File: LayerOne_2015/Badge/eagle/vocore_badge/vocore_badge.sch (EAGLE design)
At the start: 22 parts, among them U1 FT232RL-BASICSSOP

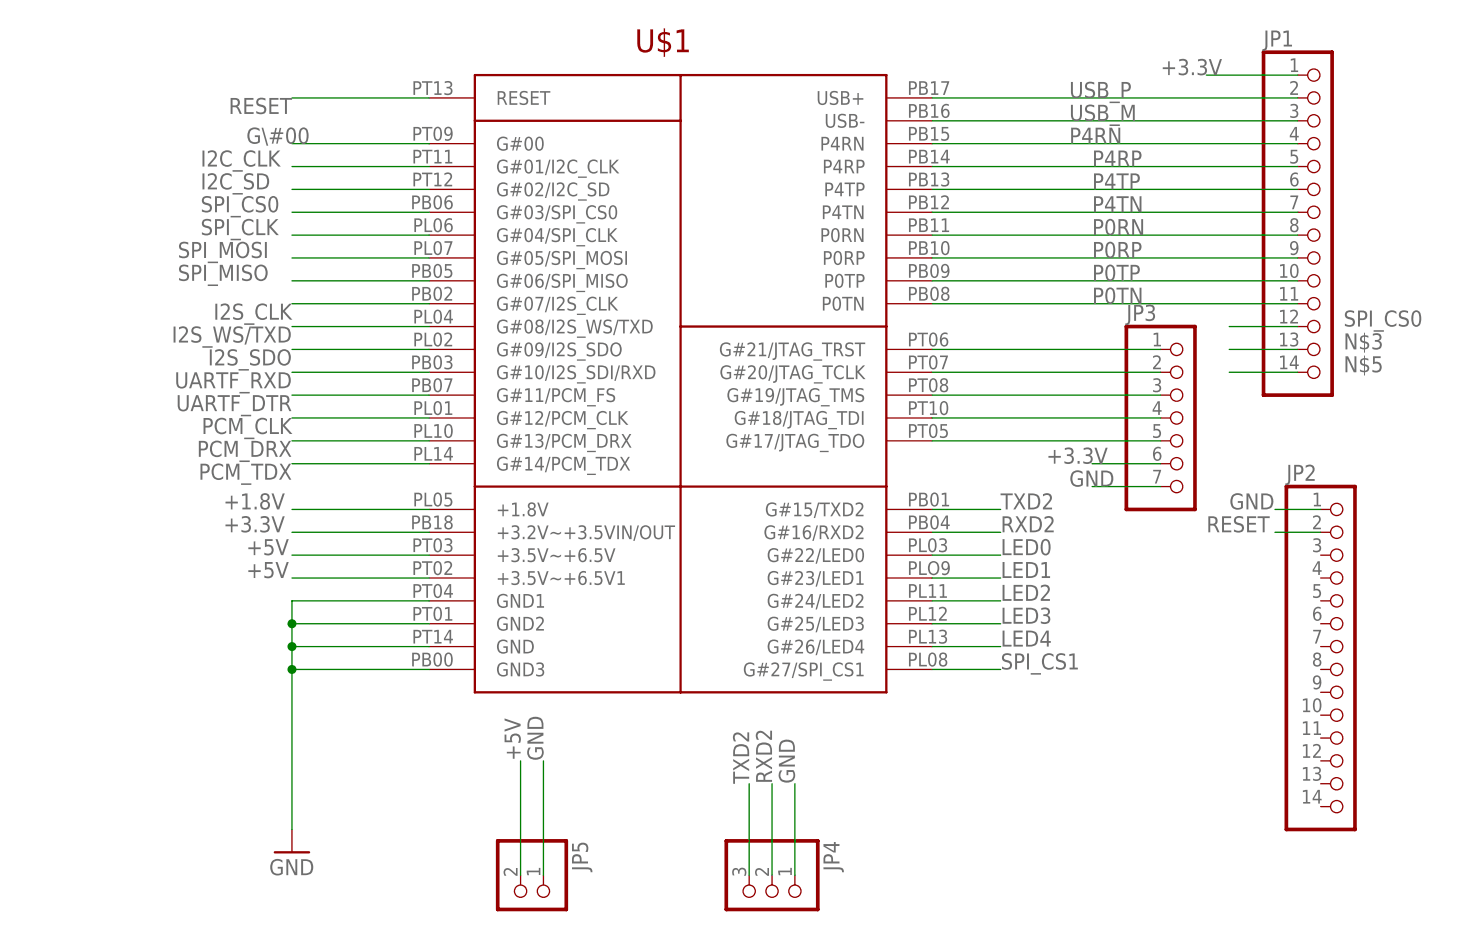
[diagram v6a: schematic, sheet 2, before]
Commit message: more breakouts on dock
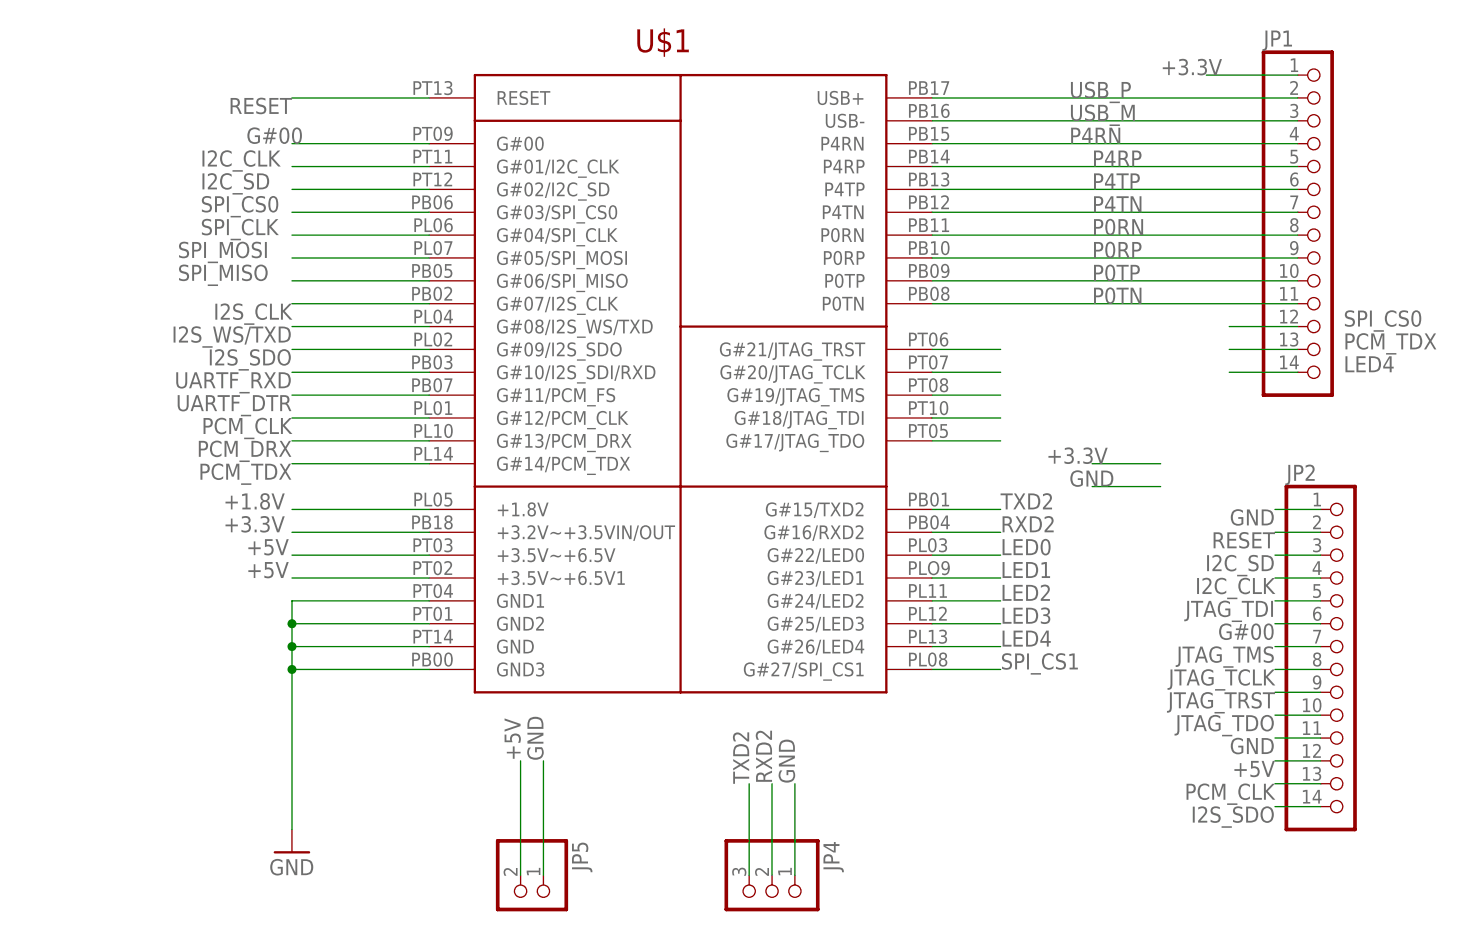
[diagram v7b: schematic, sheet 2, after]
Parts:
- removed JP3: (no value), microbuilder:HEADER-1X7ROUND
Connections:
- removed net G\#00: U$1.G#00
- removed net N$3: JP1.13
- removed net N$5: JP1.14
- new net G#00: JP2.6, U$1.G#00
- net +3.3V: no longer JP3.6
- net +5V: now also JP2.12
- net GND: now also JP2.11; no longer JP3.7
- net I2C_CLK: now also JP2.4
- net I2C_SD: now also JP2.3
- net I2S_SDO: now also JP2.14
- net JTAG_TCLK: now also JP2.8; no longer JP3.2
- net JTAG_TDI: now also JP2.5; no longer JP3.4
- net JTAG_TDO: now also JP2.10; no longer JP3.5
- net JTAG_TMS: now also JP2.7; no longer JP3.3
- net JTAG_TRST: now also JP2.9; no longer JP3.1
- net LED1: no longer R10.2
- net LED2: now also R10.2; no longer R9.1
- net LED3: now also R9.1
- net LED4: now also JP1.14
- net PCM_CLK: now also JP2.13
- net PCM_TDX: now also JP1.13
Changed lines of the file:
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@@
 <part name="JP1" library="adafruit" deviceset="PINHD-1X14" device=""/>
 <part name="JP2" library="adafruit" deviceset="PINHD-1X14" device=""/>
-<part name="JP3" library="microbuilder" deviceset="HEADER-1X7" device="ROUND"/>
 <part name="U1" library="SparkFun" deviceset="FT232RL-BASIC" device="SSOP"/>
 <part name="GND12" library="supply1" deviceset="GND" device=""/>
@@
 </segment>
 </net>
+<net name="LED3" class="0">
+<segment>
+<pinref part="R9" gate="G$1" pin="1"/>
+<wire x1="-93.98" y1="231.14" x2="-93.98" y2="238.76" width="0.1524" layer="91"/>
+</segment>
+</net>
 <net name="LED2" class="0">
 <segment>
-<pinref part="R9" gate="G$1" pin="1"/>
-<wire x1="-93.98" y1="231.14" x2="-93.98" y2="236.22" width="0.1524" layer="91"/>
-</segment>
-</net>
-<net name="LED1" class="0">
-<segment>
 <pinref part="R10" gate="G$1" pin="2"/>
-<wire x1="-104.14" y1="137.16" x2="-104.14" y2="132.08" width="0.1524" layer="91"/>
+<wire x1="-104.14" y1="137.16" x2="-104.14" y2="129.54" width="0.1524" layer="91"/>
 </segment>
 </net>
@@
 <instance part="JP1" gate="A" x="152.4" y="68.58"/>
 <instance part="JP2" gate="A" x="154.94" y="20.32"/>
-<instance part="JP3" gate="A" x="137.16" y="45.72"/>
 <instance part="JP4" gate="A" x="91.44" y="-7.62" rot="R270"/>
 <instance part="JP5" gate="G$1" x="63.5" y="-7.62" rot="R270"/>
@@
 <pinref part="JP2" gate="A" pin="1"/>
 <wire x1="152.4" y1="35.56" x2="147.32" y2="35.56" width="0.1524" layer="91"/>
-<label x="142.24" y="35.56" size="1.778" layer="95"/>
+<label x="147.32" y="35.56" size="1.778" layer="95" rot="R180"/>
 </segment>
 <segment>
 <wire x1="134.62" y1="38.1" x2="127" y2="38.1" width="0.1524" layer="91"/>
 <label x="124.46" y="38.1" size="1.778" layer="95"/>
-<pinref part="JP3" gate="A" pin="7"/>
 </segment>
 <segment>
@@
 <wire x1="66.04" y1="-5.08" x2="66.04" y2="7.62" width="0.1524" layer="91"/>
 <label x="66.04" y="7.62" size="1.778" layer="95" rot="R90"/>
+</segment>
+<segment>
+<pinref part="JP2" gate="A" pin="11"/>
+<wire x1="152.4" y1="10.16" x2="147.32" y2="10.16" width="0.1524" layer="91"/>
+<label x="147.32" y="10.16" size="1.778" layer="95" rot="R180"/>
 </segment>
 </net>
@@
 <label x="63.5" y="7.62" size="1.778" layer="95" rot="R90"/>
 </segment>
+<segment>
+<pinref part="JP2" gate="A" pin="12"/>
+<wire x1="152.4" y1="7.62" x2="147.32" y2="7.62" width="0.1524" layer="91"/>
+<label x="147.32" y="7.62" size="1.778" layer="95" rot="R180"/>
+</segment>
 </net>
 <net name="UARTF_DTR" class="0">
@@
 <wire x1="134.62" y1="40.64" x2="127" y2="40.64" width="0.1524" layer="91"/>
 <label x="121.92" y="40.64" size="1.778" layer="95"/>
-<pinref part="JP3" gate="A" pin="6"/>
 </segment>
 </net>
@@
 <label x="27.94" y="73.66" size="1.778" layer="95"/>
 </segment>
+<segment>
+<pinref part="JP2" gate="A" pin="4"/>
+<wire x1="152.4" y1="27.94" x2="147.32" y2="27.94" width="0.1524" layer="91"/>
+<label x="147.32" y="27.94" size="1.778" layer="95" rot="R180"/>
+</segment>
 </net>
 <net name="TXD2" class="0">
@@
 </segment>
 </net>
-<net name="G\#00" class="0">
+<net name="G#00" class="0">
 <segment>
 <pinref part="U$1" gate="G$1" pin="G#00"/>
@@
 <label x="33.02" y="76.2" size="1.778" layer="95"/>
 </segment>
+<segment>
+<pinref part="JP2" gate="A" pin="6"/>
+<wire x1="152.4" y1="22.86" x2="147.32" y2="22.86" width="0.1524" layer="91"/>
+<label x="147.32" y="22.86" size="1.778" layer="95" rot="R180"/>
+</segment>
 </net>
 <net name="I2C_SD" class="0">
@@
 <label x="27.94" y="71.12" size="1.778" layer="95"/>
 </segment>
+<segment>
+<pinref part="JP2" gate="A" pin="3"/>
+<wire x1="152.4" y1="30.48" x2="147.32" y2="30.48" width="0.1524" layer="91"/>
+<label x="147.32" y="30.48" size="1.778" layer="95" rot="R180"/>
+</segment>
 </net>
 <net name="SPI_CS0" class="0">
@@
 <label x="38.1" y="45.72" size="1.778" layer="95" rot="R180"/>
 </segment>
+<segment>
+<pinref part="JP2" gate="A" pin="13"/>
+<wire x1="152.4" y1="5.08" x2="147.32" y2="5.08" width="0.1524" layer="91"/>
+<label x="147.32" y="5.08" size="1.778" layer="95" rot="R180"/>
+</segment>
 </net>
 <net name="I2S_SDO" class="0">
@@
 <label x="38.1" y="53.34" size="1.778" layer="95" rot="R180"/>
 </segment>
+<segment>
+<pinref part="JP2" gate="A" pin="14"/>
+<wire x1="152.4" y1="2.54" x2="147.32" y2="2.54" width="0.1524" layer="91"/>
+<label x="147.32" y="2.54" size="1.778" layer="95" rot="R180"/>
+</segment>
 </net>
 <net name="PCM_DRX" class="0">
@@
 <label x="38.1" y="40.64" size="1.778" layer="95" rot="R180"/>
 </segment>
+<segment>
+<pinref part="JP1" gate="A" pin="13"/>
+<wire x1="149.86" y1="53.34" x2="142.24" y2="53.34" width="0.1524" layer="91"/>
+<label x="154.94" y="53.34" size="1.778" layer="95"/>
+</segment>
 </net>
 <net name="JTAG_TRST" class="0">
 <segment>
 <pinref part="U$1" gate="G$1" pin="G#21/JTAG_TRST"/>
-<wire x1="109.22" y1="53.34" x2="134.62" y2="53.34" width="0.1524" layer="91"/>
-<pinref part="JP3" gate="A" pin="1"/>
+<wire x1="109.22" y1="53.34" x2="116.84" y2="53.34" width="0.1524" layer="91"/>
+</segment>
+<segment>
+<pinref part="JP2" gate="A" pin="9"/>
+<wire x1="152.4" y1="15.24" x2="147.32" y2="15.24" width="0.1524" layer="91"/>
+<label x="147.32" y="15.24" size="1.778" layer="95" rot="R180"/>
 </segment>
 </net>
@@
 <segment>
 <pinref part="U$1" gate="G$1" pin="G#20/JTAG_TCLK"/>
-<wire x1="109.22" y1="50.8" x2="134.62" y2="50.8" width="0.1524" layer="91"/>
-<pinref part="JP3" gate="A" pin="2"/>
+<wire x1="109.22" y1="50.8" x2="116.84" y2="50.8" width="0.1524" layer="91"/>
+</segment>
+<segment>
+<pinref part="JP2" gate="A" pin="8"/>
+<wire x1="152.4" y1="17.78" x2="147.32" y2="17.78" width="0.1524" layer="91"/>
+<label x="147.32" y="17.78" size="1.778" layer="95" rot="R180"/>
 </segment>
 </net>
@@
 <segment>
 <pinref part="U$1" gate="G$1" pin="G#19/JTAG_TMS"/>
-<wire x1="109.22" y1="48.26" x2="134.62" y2="48.26" width="0.1524" layer="91"/>
-<pinref part="JP3" gate="A" pin="3"/>
+<wire x1="109.22" y1="48.26" x2="116.84" y2="48.26" width="0.1524" layer="91"/>
+</segment>
+<segment>
+<pinref part="JP2" gate="A" pin="7"/>
+<wire x1="152.4" y1="20.32" x2="147.32" y2="20.32" width="0.1524" layer="91"/>
+<label x="147.32" y="20.32" size="1.778" layer="95" rot="R180"/>
 </segment>
 </net>
@@
 <segment>
 <pinref part="U$1" gate="G$1" pin="G#18/JTAG_TDI"/>
-<wire x1="109.22" y1="45.72" x2="134.62" y2="45.72" width="0.1524" layer="91"/>
-<pinref part="JP3" gate="A" pin="4"/>
+<wire x1="109.22" y1="45.72" x2="116.84" y2="45.72" width="0.1524" layer="91"/>
+</segment>
+<segment>
+<pinref part="JP2" gate="A" pin="5"/>
+<wire x1="152.4" y1="25.4" x2="147.32" y2="25.4" width="0.1524" layer="91"/>
+<label x="147.32" y="25.4" size="1.778" layer="95" rot="R180"/>
 </segment>
 </net>
@@
 <segment>
 <pinref part="U$1" gate="G$1" pin="G#17/JTAG_TDO"/>
-<wire x1="109.22" y1="43.18" x2="134.62" y2="43.18" width="0.1524" layer="91"/>
-<pinref part="JP3" gate="A" pin="5"/>
+<wire x1="109.22" y1="43.18" x2="116.84" y2="43.18" width="0.1524" layer="91"/>
+</segment>
+<segment>
+<pinref part="JP2" gate="A" pin="10"/>
+<wire x1="152.4" y1="12.7" x2="147.32" y2="12.7" width="0.1524" layer="91"/>
+<label x="147.32" y="12.7" size="1.778" layer="95" rot="R180"/>
 </segment>
 </net>
@@
 <label x="116.84" y="20.32" size="1.778" layer="95"/>
 </segment>
+<segment>
+<pinref part="JP1" gate="A" pin="14"/>
+<wire x1="149.86" y1="50.8" x2="142.24" y2="50.8" width="0.1524" layer="91"/>
+<label x="154.94" y="50.8" size="1.778" layer="95"/>
+</segment>
 </net>
 <net name="RESET" class="0">
@@
 <wire x1="152.4" y1="33.02" x2="147.32" y2="33.02" width="0.1524" layer="91"/>
 <pinref part="JP2" gate="A" pin="2"/>
-<label x="139.7" y="33.02" size="1.778" layer="95"/>
-</segment>
-</net>
-<net name="N$3" class="0">
-<segment>
-<pinref part="JP1" gate="A" pin="13"/>
-<wire x1="149.86" y1="53.34" x2="142.24" y2="53.34" width="0.1524" layer="91"/>
-<label x="154.94" y="53.34" size="1.778" layer="95"/>
-</segment>
-</net>
-<net name="N$5" class="0">
-<segment>
-<pinref part="JP1" gate="A" pin="14"/>
-<wire x1="149.86" y1="50.8" x2="142.24" y2="50.8" width="0.1524" layer="91"/>
-<label x="154.94" y="50.8" size="1.778" layer="95"/>
-</segment>
-</net>
+<label x="147.32" y="33.02" size="1.778" layer="95" rot="R180"/>
+</segment>
+</net>

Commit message: 20k SDCARD
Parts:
- R3, R4, R5, R6, R7, R8: value (none) -> 20K
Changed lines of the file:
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@@
 <part name="R1" library="SparkFun-Resistors" deviceset="RESISTOR" device="0805-RES" value="150R"/>
 <part name="R2" library="SparkFun-Resistors" deviceset="RESISTOR" device="0805-RES" value="150"/>
-<part name="R3" library="SparkFun-Resistors" deviceset="RESISTOR" device="0805-RES"/>
-<part name="R4" library="SparkFun-Resistors" deviceset="RESISTOR" device="0805-RES"/>
-<part name="R5" library="SparkFun-Resistors" deviceset="RESISTOR" device="0805-RES"/>
-<part name="R6" library="SparkFun-Resistors" deviceset="RESISTOR" device="0805-RES"/>
-<part name="R7" library="SparkFun-Resistors" deviceset="RESISTOR" device="0805-RES"/>
-<part name="R8" library="SparkFun-Resistors" deviceset="RESISTOR" device="0805-RES"/>
+<part name="R3" library="SparkFun-Resistors" deviceset="RESISTOR" device="0805-RES" value="20K"/>
+<part name="R4" library="SparkFun-Resistors" deviceset="RESISTOR" device="0805-RES" value="20K"/>
+<part name="R5" library="SparkFun-Resistors" deviceset="RESISTOR" device="0805-RES" value="20K"/>
+<part name="R6" library="SparkFun-Resistors" deviceset="RESISTOR" device="0805-RES" value="20K"/>
+<part name="R7" library="SparkFun-Resistors" deviceset="RESISTOR" device="0805-RES" value="20K"/>
+<part name="R8" library="SparkFun-Resistors" deviceset="RESISTOR" device="0805-RES" value="20K"/>
 <part name="USB1" library="vocore_dock" deviceset="USB_MICRO_A" device="USB_MICRO_A" value="USB_MICRO_A"/>
 <part name="GND4" library="supply1" deviceset="GND" device=""/>
